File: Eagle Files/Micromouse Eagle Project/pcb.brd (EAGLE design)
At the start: 108.9 x 81.3 mm, 19 parts, among them Q1 IRF540

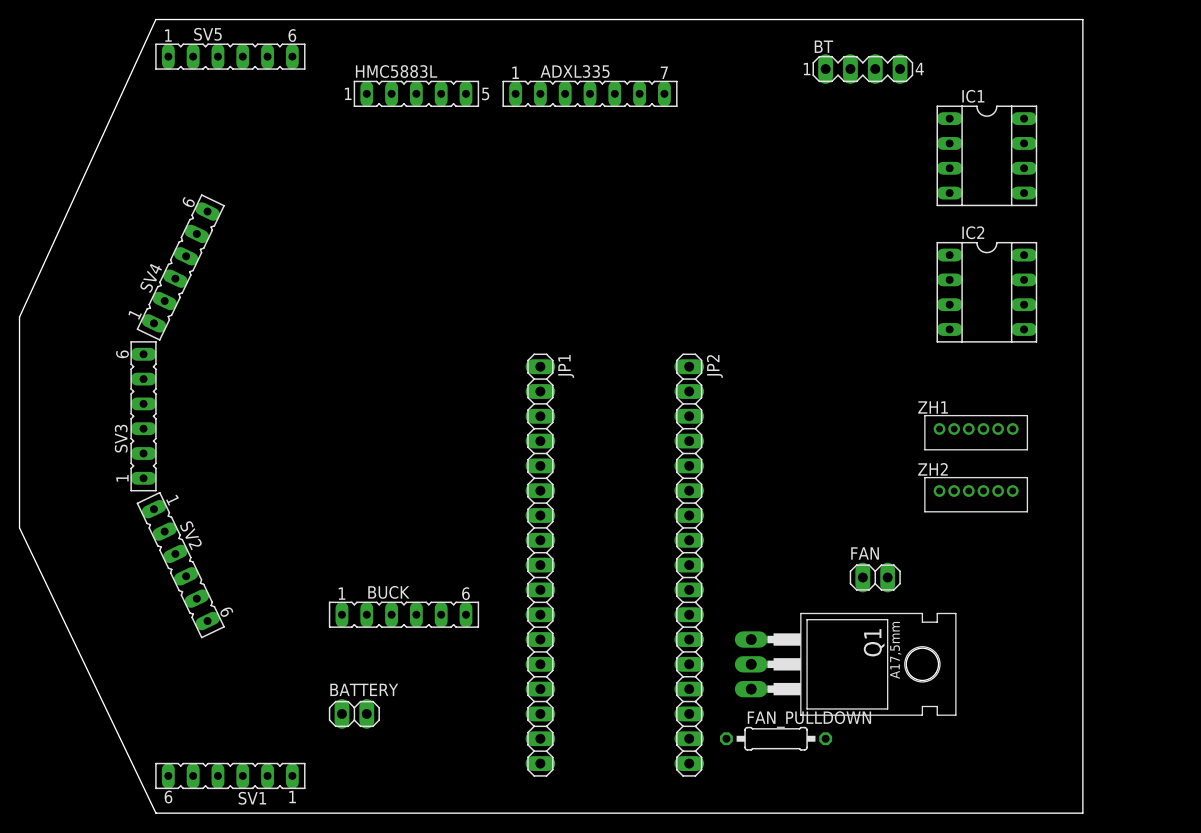
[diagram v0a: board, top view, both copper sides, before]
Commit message: added labels
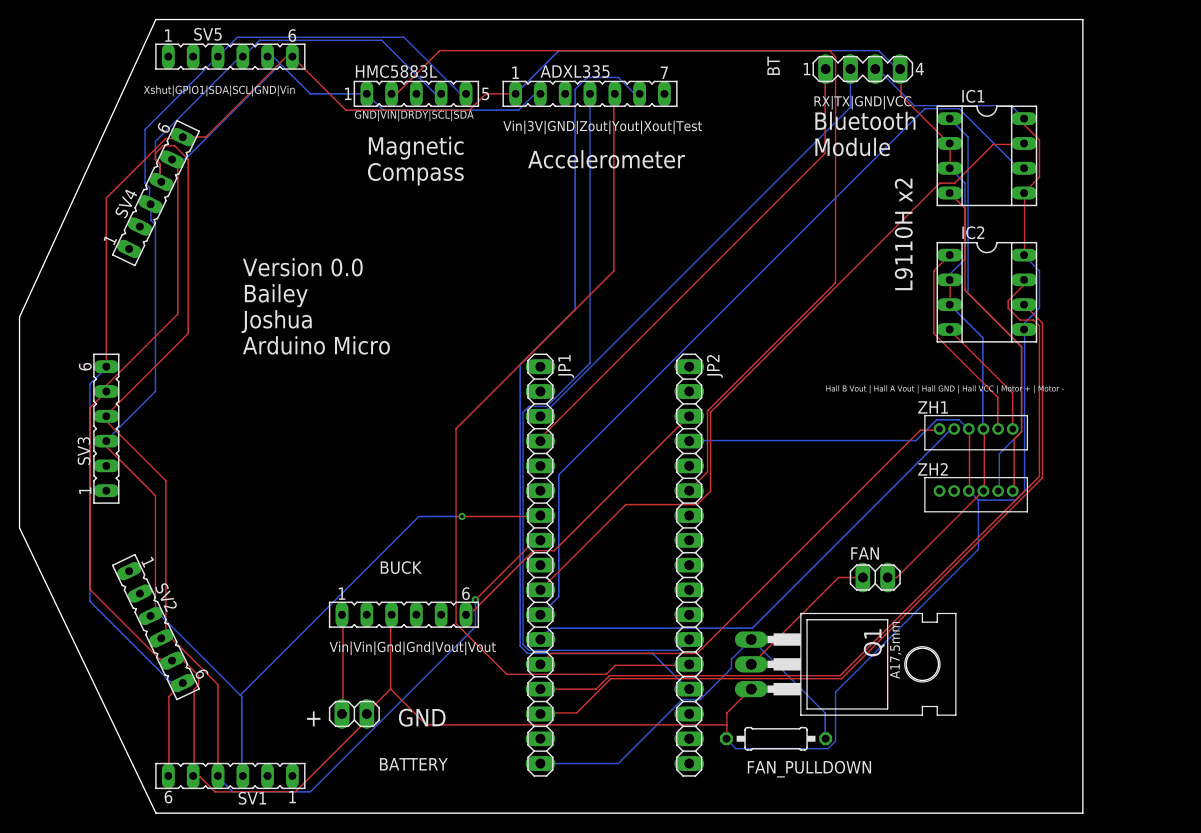
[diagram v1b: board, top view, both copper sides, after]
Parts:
- moved SV4 8.03 mm to (5.08, 62.2)
- moved SV2 6.84 mm to (5.08, 17.8)
- moved SV3 4.02 mm to (0.00, 38.1)
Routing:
- net GND: track 0.00 -> 338.6 mm
- net VCC: track 0.00 -> 219.8 mm
- net SCL: track 0.00 -> 166.4 mm, vias 0 -> 1
- net SDA: track 0.00 -> 153.1 mm, vias 0 -> 1
- net VCC-ARDUINO: track 0.00 -> 98.2 mm
- net A1: track 0.00 -> 87.5 mm
- net A0: track 0.00 -> 86.3 mm
- net 9: track 0.00 -> 83.1 mm
- net 6: track 0.00 -> 80.8 mm
- net 10: track 0.00 -> 80.0 mm
- net A2: track 0.00 -> 78.0 mm
- net 5: track 0.00 -> 73.2 mm
- net HALLB_1: track 0.00 -> 51.3 mm
- net HALLA_1: track 0.00 -> 50.9 mm
- net RX: track 0.00 -> 50.2 mm
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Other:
- board text added: "+ GND"
- board text added: "Accelerometer"
- board text added: "Bluetooth Module"
- board text added: "GND|VIN|DRDY|SCL|SDA"
- board text added: "Hall B Vout | Hall A Vout | Hall GND | Hall VCC | Motor + | Motor -"
- board text added: "L9110H x2"
- board text added: "Magnetic Compass"
- board text added: "RX|TX|GND|VCC"
- board text added: "Version 0.0 Bailey Joshua Arduino Micro"
- board text added: "Vin|3V|GND|Zout|Yout|Xout|Test"
- board text added: "Vin|Vin|Gnd|Gnd|Vout|Vout"
- board text added: "Xshut|GPIO1|SDA|SCL|GND|Vin"
